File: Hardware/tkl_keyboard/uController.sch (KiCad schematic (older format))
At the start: 15 parts, among them J3 Conn_02x03_Odd_Even, SW1 SW_Push, U5 ATmega32U4-AU, X2 KC2016K

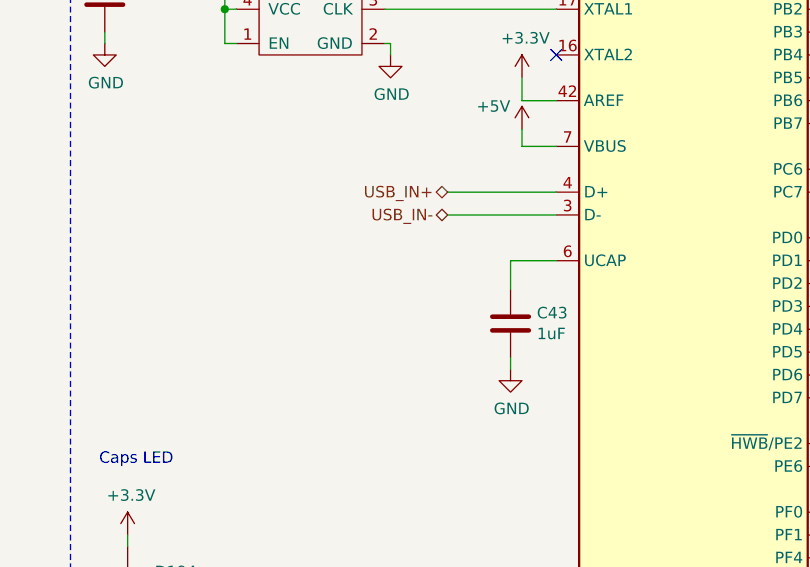
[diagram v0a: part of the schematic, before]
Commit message: Fixing USB circuit, adding data line resistors as per AN-5052
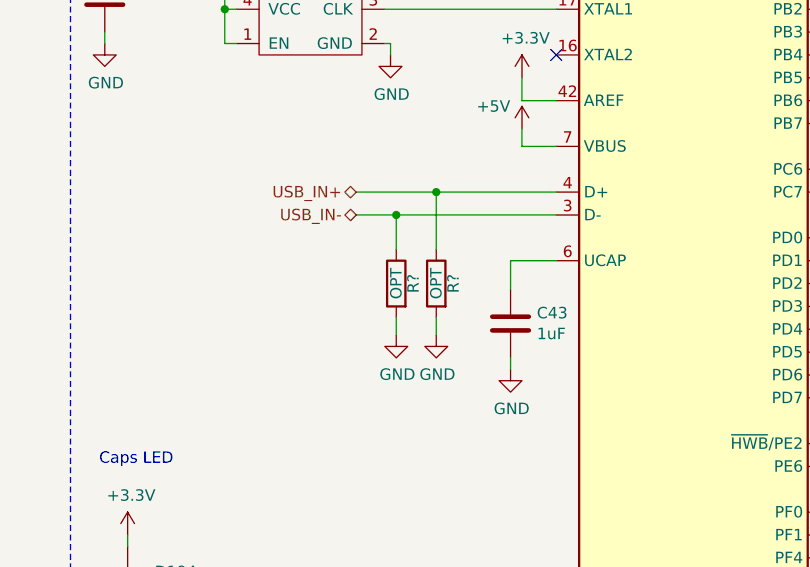
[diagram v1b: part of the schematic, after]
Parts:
- added R? (x2): OPT, resistor_smd:R_0603_1608Metric, symbol Device:R
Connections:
- net GND: now also R?.2, R?.2
- net USB_IN+: now also R?.1
- net USB_IN-: now also R?.1
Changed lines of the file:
@@
 	5925 3525 5575 3525
-Wire Wire Line
-	3900 3625 4375 3625
-Wire Wire Line
-	3900 3725 4375 3725
 Wire Wire Line
 	2975 2975 2925 2975
@@
 Wire Notes Line
 	6650 2900 8300 2900
-Text HLabel 3900 3625 0    50   BiDi ~ 0
+Text HLabel 3500 3625 0    50   BiDi ~ 0
 USB_IN+
-Text HLabel 3900 3725 0    50   BiDi ~ 0
+Text HLabel 3500 3725 0    50   BiDi ~ 0
 USB_IN-
 Text HLabel 5925 3625 2    50   BiDi ~ 0
@@
 Wire Wire Line
 	2675 5900 2500 5900
+$Comp
+L Device:R R?
+U 1 1 614C2CC6
+P 3675 4025
+AR Path="/6114D32E/614C2CC6" Ref="R?"  Part="1"
+AR Path="/6247A5CE/614C2CC6" Ref="R?"  Part="1"
+AR Path="/61234350/614C2CC6" Ref="R?"  Part="1"
+AR Path="/62FAC6FD/614C2CC6" Ref="R?"  Part="1"
+AR Path="/650FF941/614C2CC6" Ref="R?"  Part="1"
+AR Path="/6511E0C5/614C2CC6" Ref="R?"  Part="1"
+AR Path="/65128D7D/614C2CC6" Ref="R?"  Part="1"
+AR Path="/63013830/614C2CC6" Ref="R?"  Part="1"
+F 0 "R?" V 3600 4025 50  0000 C CNN
+F 1 "OPT" V 3675 4025 50  0000 C CNN
+F 2 "resistor_smd:R_0603_1608Metric" V 3605 4025 50  0001 C CNN
+F 3 "~" H 3675 4025 50  0001 C CNN
+	1    3675 4025
+	-1   0    0    -1
+$EndComp
+$Comp
+L Device:R R?
+U 1 1 614C2CCC
+P 3850 4025
+AR Path="/6114D32E/614C2CCC" Ref="R?"  Part="1"
+AR Path="/6247A5CE/614C2CCC" Ref="R?"  Part="1"
+AR Path="/61234350/614C2CCC" Ref="R?"  Part="1"
+AR Path="/62FAC6FD/614C2CCC" Ref="R?"  Part="1"
+AR Path="/650FF941/614C2CCC" Ref="R?"  Part="1"
+AR Path="/6511E0C5/614C2CCC" Ref="R?"  Part="1"
+AR Path="/65128D7D/614C2CCC" Ref="R?"  Part="1"
+AR Path="/63013830/614C2CCC" Ref="R?"  Part="1"
+F 0 "R?" V 3775 4025 50  0000 C CNN
+F 1 "OPT" V 3850 4025 50  0000 C CNN
+F 2 "resistor_smd:R_0603_1608Metric" V 3780 4025 50  0001 C CNN
+F 3 "~" H 3850 4025 50  0001 C CNN
+	1    3850 4025
+	-1   0    0    -1
+$EndComp
+$Comp
+L power:GND #PWR?
+U 1 1 614C2CD2
+P 3675 4250
+AR Path="/6114D32E/614C2CD2" Ref="#PWR?"  Part="1"
+AR Path="/6247A5CE/614C2CD2" Ref="#PWR?"  Part="1"
+AR Path="/61234350/614C2CD2" Ref="#PWR?"  Part="1"
+AR Path="/62FAC6FD/614C2CD2" Ref="#PWR?"  Part="1"
+AR Path="/650FF941/614C2CD2" Ref="#PWR?"  Part="1"
+AR Path="/6511E0C5/614C2CD2" Ref="#PWR?"  Part="1"
+AR Path="/65128D7D/614C2CD2" Ref="#PWR?"  Part="1"
+F 0 "#PWR?" H 3675 4000 50  0001 C CNN
+F 1 "GND" H 3680 4077 50  0000 C CNN
+F 2 "" H 3675 4250 50  0001 C CNN
+F 3 "" H 3675 4250 50  0001 C CNN
+	1    3675 4250
+	1    0    0    -1
+$EndComp
+$Comp
+L power:GND #PWR?
+U 1 1 614C2CD8
+P 3850 4250
+AR Path="/6114D32E/614C2CD8" Ref="#PWR?"  Part="1"
+AR Path="/6247A5CE/614C2CD8" Ref="#PWR?"  Part="1"
+AR Path="/61234350/614C2CD8" Ref="#PWR?"  Part="1"
+AR Path="/62FAC6FD/614C2CD8" Ref="#PWR?"  Part="1"
+AR Path="/650FF941/614C2CD8" Ref="#PWR?"  Part="1"
+AR Path="/6511E0C5/614C2CD8" Ref="#PWR?"  Part="1"
+AR Path="/65128D7D/614C2CD8" Ref="#PWR?"  Part="1"
+F 0 "#PWR?" H 3850 4000 50  0001 C CNN
+F 1 "GND" H 3855 4077 50  0000 C CNN
+F 2 "" H 3850 4250 50  0001 C CNN
+F 3 "" H 3850 4250 50  0001 C CNN
+	1    3850 4250
+	1    0    0    -1
+$EndComp
+Wire Wire Line
+	3675 4250 3675 4175
+Wire Wire Line
+	3850 4250 3850 4175
+Wire Wire Line
+	3500 3625 3850 3625
+Wire Wire Line
+	3500 3725 3675 3725
+Wire Wire Line
+	3675 3875 3675 3725
+Connection ~ 3675 3725
+Wire Wire Line
+	3675 3725 4375 3725
+Wire Wire Line
+	3850 3875 3850 3625
+Connection ~ 3850 3625
+Wire Wire Line
+	3850 3625 4375 3625
 $EndSCHEMATC

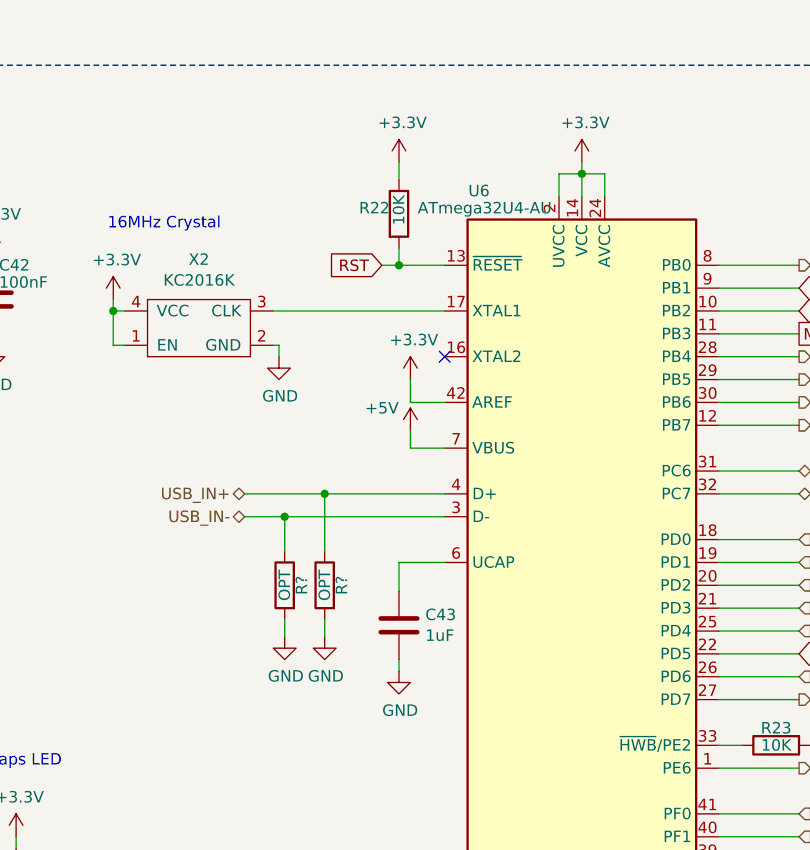
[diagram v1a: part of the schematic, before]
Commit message: Tidying schematic
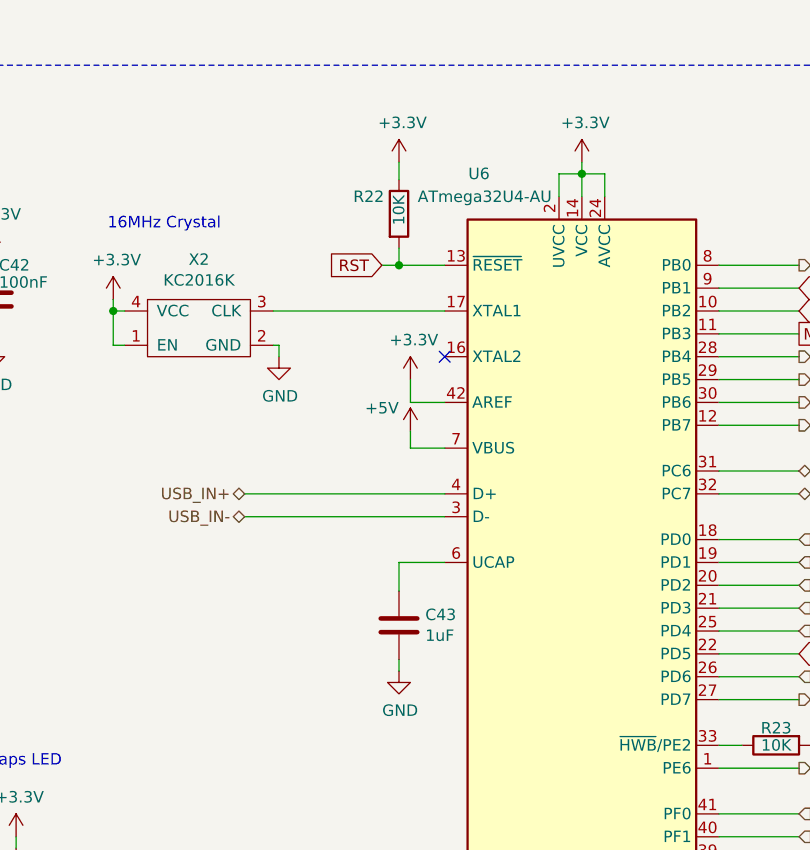
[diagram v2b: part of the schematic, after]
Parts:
- removed R? (x2): OPT, resistor_smd:R_0603_1608Metric, symbol Device:R
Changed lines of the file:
@@
 encoding utf-8
 Sheet 4 12
-Title ""
+Title "TKL Keyboard"
 Date ""
-Rev ""
+Rev "0"
 Comp ""
 Comment1 ""
@@
 AR Path="/612342D1/60D69247" Ref="U5"  Part="1"
 AR Path="/63013830/60D69247" Ref="U6"  Part="1"
-F 0 "U6" H 4525 5950 50  0000 C CNN
-F 1 "ATmega32U4-AU" H 4550 5875 50  0000 C CNN
+F 0 "U6" H 4525 6025 50  0000 C CNN
+F 1 "ATmega32U4-AU" H 4550 5925 50  0000 C CNN
 F 2 "Package_QFP:TQFP-44_10x10mm_P0.8mm" H 4975 4125 50  0001 C CIN
 F 3 "http://ww1.microchip.com/downloads/en/DeviceDoc/Atmel-7766-8-bit-AVR-ATmega16U4-32U4_Datasheet.pdf" H 4975 4125 50  0001 C CNN
@@
 AR Path="/612342D1/60D6927E" Ref="R18"  Part="1"
 AR Path="/63013830/60D6927E" Ref="R22"  Part="1"
-F 0 "R22" H 4000 2425 50  0000 L CNN
+F 0 "R22" H 3975 2475 50  0000 L CNN
 F 1 "10K" V 4175 2350 50  0000 L CNN
 F 2 "resistor_smd:R_0603_1608Metric" V 4105 2400 50  0001 C CNN
@@
 Wire Wire Line
 	2675 5900 2500 5900
-$Comp
-L Device:R R?
-U 1 1 614C2CC6
-P 3675 4025
-AR Path="/6114D32E/614C2CC6" Ref="R?"  Part="1"
-AR Path="/6247A5CE/614C2CC6" Ref="R?"  Part="1"
-AR Path="/61234350/614C2CC6" Ref="R?"  Part="1"
-AR Path="/62FAC6FD/614C2CC6" Ref="R?"  Part="1"
-AR Path="/650FF941/614C2CC6" Ref="R?"  Part="1"
-AR Path="/6511E0C5/614C2CC6" Ref="R?"  Part="1"
-AR Path="/65128D7D/614C2CC6" Ref="R?"  Part="1"
-AR Path="/63013830/614C2CC6" Ref="R?"  Part="1"
-F 0 "R?" V 3600 4025 50  0000 C CNN
-F 1 "OPT" V 3675 4025 50  0000 C CNN
-F 2 "resistor_smd:R_0603_1608Metric" V 3605 4025 50  0001 C CNN
-F 3 "~" H 3675 4025 50  0001 C CNN
-	1    3675 4025
-	-1   0    0    -1
-$EndComp
-$Comp
-L Device:R R?
-U 1 1 614C2CCC
-P 3850 4025
-AR Path="/6114D32E/614C2CCC" Ref="R?"  Part="1"
-AR Path="/6247A5CE/614C2CCC" Ref="R?"  Part="1"
-AR Path="/61234350/614C2CCC" Ref="R?"  Part="1"
-AR Path="/62FAC6FD/614C2CCC" Ref="R?"  Part="1"
-AR Path="/650FF941/614C2CCC" Ref="R?"  Part="1"
-AR Path="/6511E0C5/614C2CCC" Ref="R?"  Part="1"
-AR Path="/65128D7D/614C2CCC" Ref="R?"  Part="1"
-AR Path="/63013830/614C2CCC" Ref="R?"  Part="1"
-F 0 "R?" V 3775 4025 50  0000 C CNN
-F 1 "OPT" V 3850 4025 50  0000 C CNN
-F 2 "resistor_smd:R_0603_1608Metric" V 3780 4025 50  0001 C CNN
-F 3 "~" H 3850 4025 50  0001 C CNN
-	1    3850 4025
-	-1   0    0    -1
-$EndComp
-$Comp
-L power:GND #PWR?
-U 1 1 614C2CD2
-P 3675 4250
-AR Path="/6114D32E/614C2CD2" Ref="#PWR?"  Part="1"
-AR Path="/6247A5CE/614C2CD2" Ref="#PWR?"  Part="1"
-AR Path="/61234350/614C2CD2" Ref="#PWR?"  Part="1"
-AR Path="/62FAC6FD/614C2CD2" Ref="#PWR?"  Part="1"
-AR Path="/650FF941/614C2CD2" Ref="#PWR?"  Part="1"
-AR Path="/6511E0C5/614C2CD2" Ref="#PWR?"  Part="1"
-AR Path="/65128D7D/614C2CD2" Ref="#PWR?"  Part="1"
-F 0 "#PWR?" H 3675 4000 50  0001 C CNN
-F 1 "GND" H 3680 4077 50  0000 C CNN
-F 2 "" H 3675 4250 50  0001 C CNN
-F 3 "" H 3675 4250 50  0001 C CNN
-	1    3675 4250
-	1    0    0    -1
-$EndComp
-$Comp
-L power:GND #PWR?
-U 1 1 614C2CD8
-P 3850 4250
-AR Path="/6114D32E/614C2CD8" Ref="#PWR?"  Part="1"
-AR Path="/6247A5CE/614C2CD8" Ref="#PWR?"  Part="1"
-AR Path="/61234350/614C2CD8" Ref="#PWR?"  Part="1"
-AR Path="/62FAC6FD/614C2CD8" Ref="#PWR?"  Part="1"
-AR Path="/650FF941/614C2CD8" Ref="#PWR?"  Part="1"
-AR Path="/6511E0C5/614C2CD8" Ref="#PWR?"  Part="1"
-AR Path="/65128D7D/614C2CD8" Ref="#PWR?"  Part="1"
-F 0 "#PWR?" H 3850 4000 50  0001 C CNN
-F 1 "GND" H 3855 4077 50  0000 C CNN
-F 2 "" H 3850 4250 50  0001 C CNN
-F 3 "" H 3850 4250 50  0001 C CNN
-	1    3850 4250
-	1    0    0    -1
-$EndComp
-Wire Wire Line
-	3675 4250 3675 4175
-Wire Wire Line
-	3850 4250 3850 4175
-Wire Wire Line
-	3500 3625 3850 3625
-Wire Wire Line
-	3500 3725 3675 3725
-Wire Wire Line
-	3675 3875 3675 3725
-Connection ~ 3675 3725
-Wire Wire Line
-	3675 3725 4375 3725
-Wire Wire Line
-	3850 3875 3850 3625
-Connection ~ 3850 3625
-Wire Wire Line
-	3850 3625 4375 3625
+Wire Wire Line
+	3500 3725 4375 3725
+Wire Wire Line
+	3500 3625 4375 3625
 $EndSCHEMATC
